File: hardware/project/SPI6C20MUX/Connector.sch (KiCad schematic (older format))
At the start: 2 parts, among them J302 Conn_02x08_Odd_Even, J501 Conn_01x06

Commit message: Software and hardware development
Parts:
- added R301, R302: 10k, Resistor_SMD:R_0603_1608Metric_Pad1.05x0.95mm_HandSolder, symbol Device:R
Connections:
- net +3V3: now also R301.1, R302.1
- net GND: now also R301.2, R302.2
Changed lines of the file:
@@
 EESchema Schematic File Version 4
-LIBS:SPI6C20MUX-cache
 EELAYER 30 0
 EELAYER END
@@
 	3550 3000 3450 3000
 NoConn ~ 3450 2700
-Wire Wire Line
-	3450 2800 3500 2800
-Wire Wire Line
-	3500 2800 3500 2900
-Wire Wire Line
-	3500 2900 3450 2900
 $Comp
 L power:+3.3V #PWR0303
 U 1 1 5DDAE9D9
-P 3550 2800
-F 0 "#PWR0303" H 3550 2650 50  0001 C CNN
-F 1 "+3.3V" V 3565 2928 50  0000 L CNN
-F 2 "" H 3550 2800 50  0001 C CNN
-F 3 "" H 3550 2800 50  0001 C CNN
-	1    3550 2800
+P 4850 2800
+F 0 "#PWR0303" H 4850 2650 50  0001 C CNN
+F 1 "+3.3V" V 4865 2928 50  0000 L CNN
+F 2 "" H 4850 2800 50  0001 C CNN
+F 3 "" H 4850 2800 50  0001 C CNN
+	1    4850 2800
 	0    1    1    0
 $EndComp
-Wire Wire Line
-	3550 2800 3500 2800
-Connection ~ 3500 2800
+$Comp
+L Device:R R301
+U 1 1 5E0C77B3
+P 4350 3100
+F 0 "R301" H 4420 3146 50  0000 L CNN
+F 1 "10k" H 4420 3055 50  0000 L CNN
+F 2 "Resistor_SMD:R_0603_1608Metric_Pad1.05x0.95mm_HandSolder" V 4280 3100 50  0001 C CNN
+F 3 "~" H 4350 3100 50  0001 C CNN
+	1    4350 3100
+	1    0    0    -1
+$EndComp
+$Comp
+L power:GND #PWR0304
+U 1 1 5E0C81D3
+P 4350 3250
+F 0 "#PWR0304" H 4350 3000 50  0001 C CNN
+F 1 "GND" H 4355 3077 50  0000 C CNN
+F 2 "" H 4350 3250 50  0001 C CNN
+F 3 "" H 4350 3250 50  0001 C CNN
+	1    4350 3250
+	1    0    0    -1
+$EndComp
+Wire Wire Line
+	4350 2950 4350 2900
+Wire Wire Line
+	3450 2900 4350 2900
+$Comp
+L Device:R R302
+U 1 1 5E0C9828
+P 4750 3100
+F 0 "R302" H 4820 3146 50  0000 L CNN
+F 1 "10k" H 4820 3055 50  0000 L CNN
+F 2 "Resistor_SMD:R_0603_1608Metric_Pad1.05x0.95mm_HandSolder" V 4680 3100 50  0001 C CNN
+F 3 "~" H 4750 3100 50  0001 C CNN
+	1    4750 3100
+	1    0    0    -1
+$EndComp
+Wire Wire Line
+	4750 2950 4750 2800
+Wire Wire Line
+	3450 2800 4750 2800
+$Comp
+L power:GND #PWR0305
+U 1 1 5E0CA1C4
+P 4750 3250
+F 0 "#PWR0305" H 4750 3000 50  0001 C CNN
+F 1 "GND" H 4755 3077 50  0000 C CNN
+F 2 "" H 4750 3250 50  0001 C CNN
+F 3 "" H 4750 3250 50  0001 C CNN
+	1    4750 3250
+	1    0    0    -1
+$EndComp
+Wire Wire Line
+	4850 2800 4750 2800
+Connection ~ 4750 2800
+$Comp
+L power:+3.3V #PWR0306
+U 1 1 5E0CA9CB
+P 4850 2900
+F 0 "#PWR0306" H 4850 2750 50  0001 C CNN
+F 1 "+3.3V" V 4865 3028 50  0000 L CNN
+F 2 "" H 4850 2900 50  0001 C CNN
+F 3 "" H 4850 2900 50  0001 C CNN
+	1    4850 2900
+	0    1    1    0
+$EndComp
+Wire Wire Line
+	4850 2900 4350 2900
+Connection ~ 4350 2900
 $EndSCHEMATC

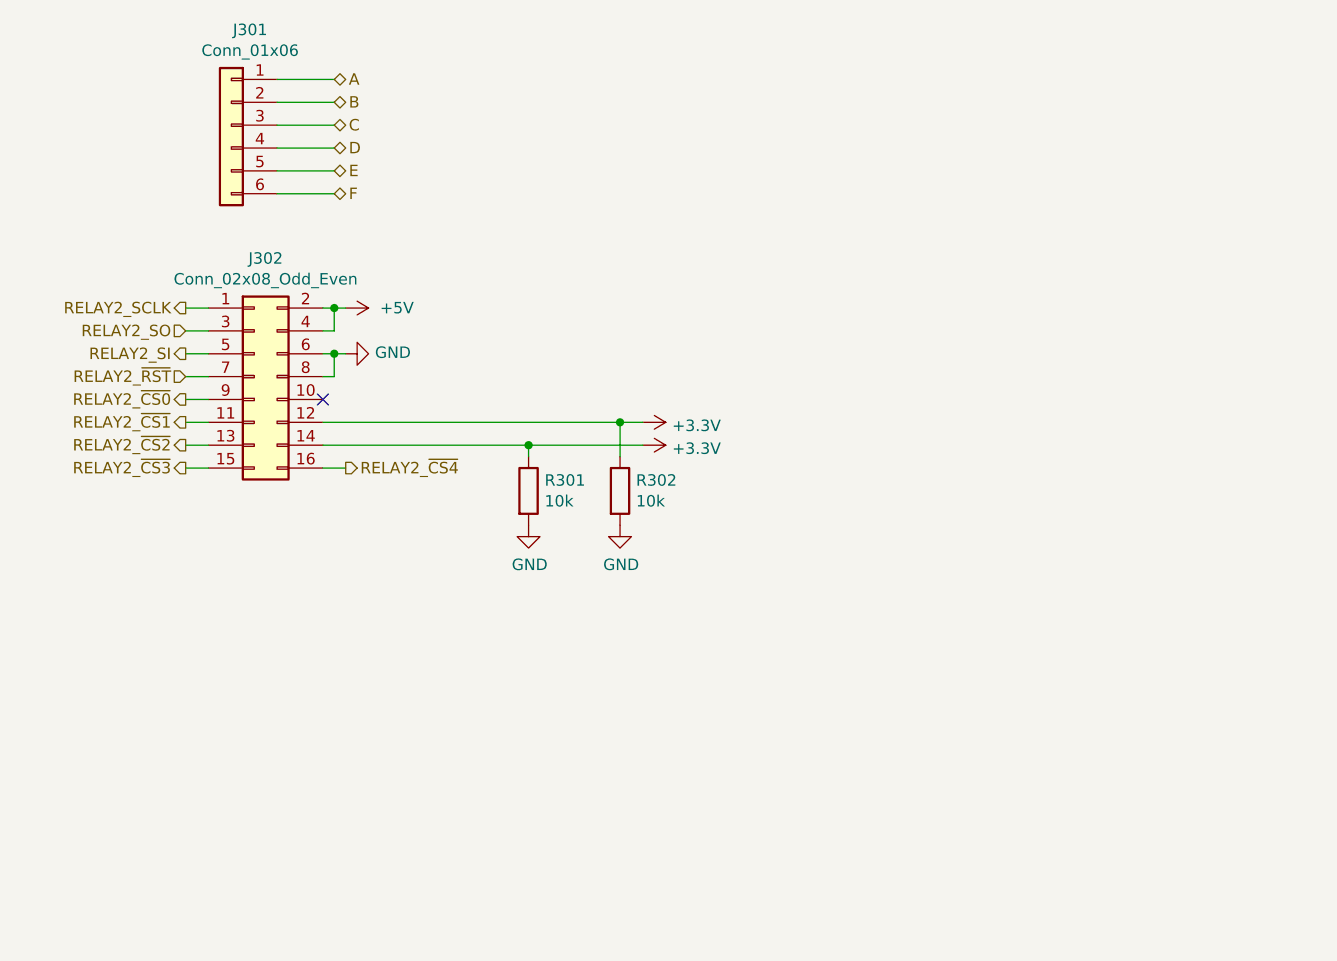
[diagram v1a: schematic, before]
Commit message: PCB main and module layout.
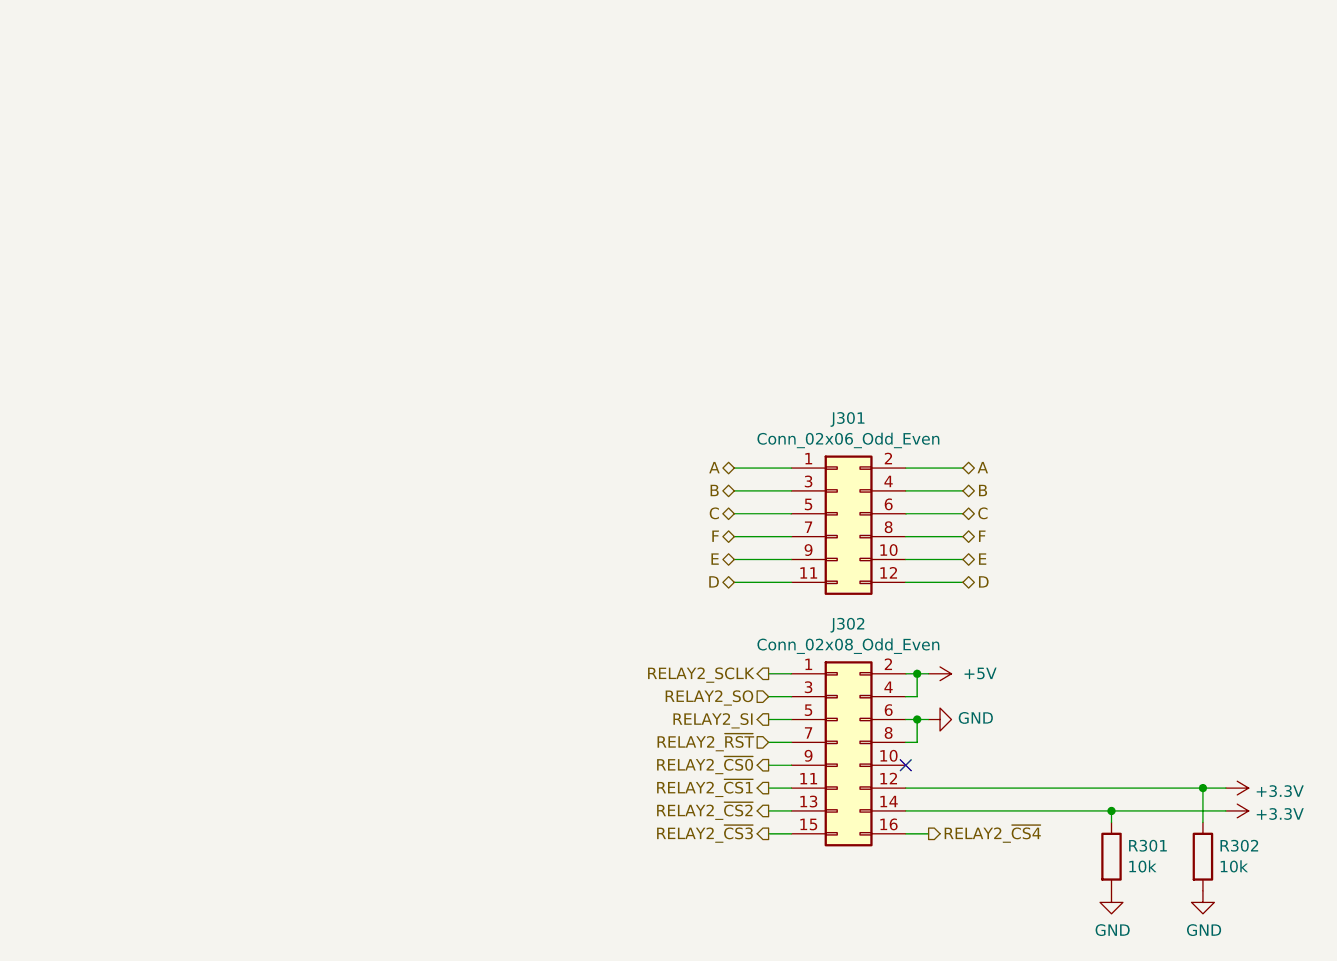
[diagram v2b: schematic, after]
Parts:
- removed J501: Conn_01x06, Connector_PinHeader_2.54mm:PinHeader_1x06_P2.54mm_Vertical, symbol Connector_Generic:Conn_01x06
- added J301: Conn_02x06_Odd_Even, Connector_PinHeader_2.54mm:PinHeader_2x06_P2.54mm_Vertical, symbol Connector_Generic:Conn_02x06_Odd_Even
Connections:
- net A: now also J301.1 (Pin_1), J301.2 (Pin_2)
- net B: now also J301.3 (Pin_3), J301.4 (Pin_4)
- net C: now also J301.5 (Pin_5), J301.6 (Pin_6)
- net D: now also J301.11 (Pin_11), J301.12 (Pin_12)
- net E: now also J301.10 (Pin_10), J301.9 (Pin_9)
- net F: now also J301.7 (Pin_7), J301.8 (Pin_8)
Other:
- moved on the sheet: J302, R301, R302
